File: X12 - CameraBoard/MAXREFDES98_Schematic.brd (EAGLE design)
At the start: 100 x 80 mm, 24 parts, among them U1 MB110S-TP, U2 MB110S-TP, U3 MAX5969AETB+, U4 MAX17503ATP+

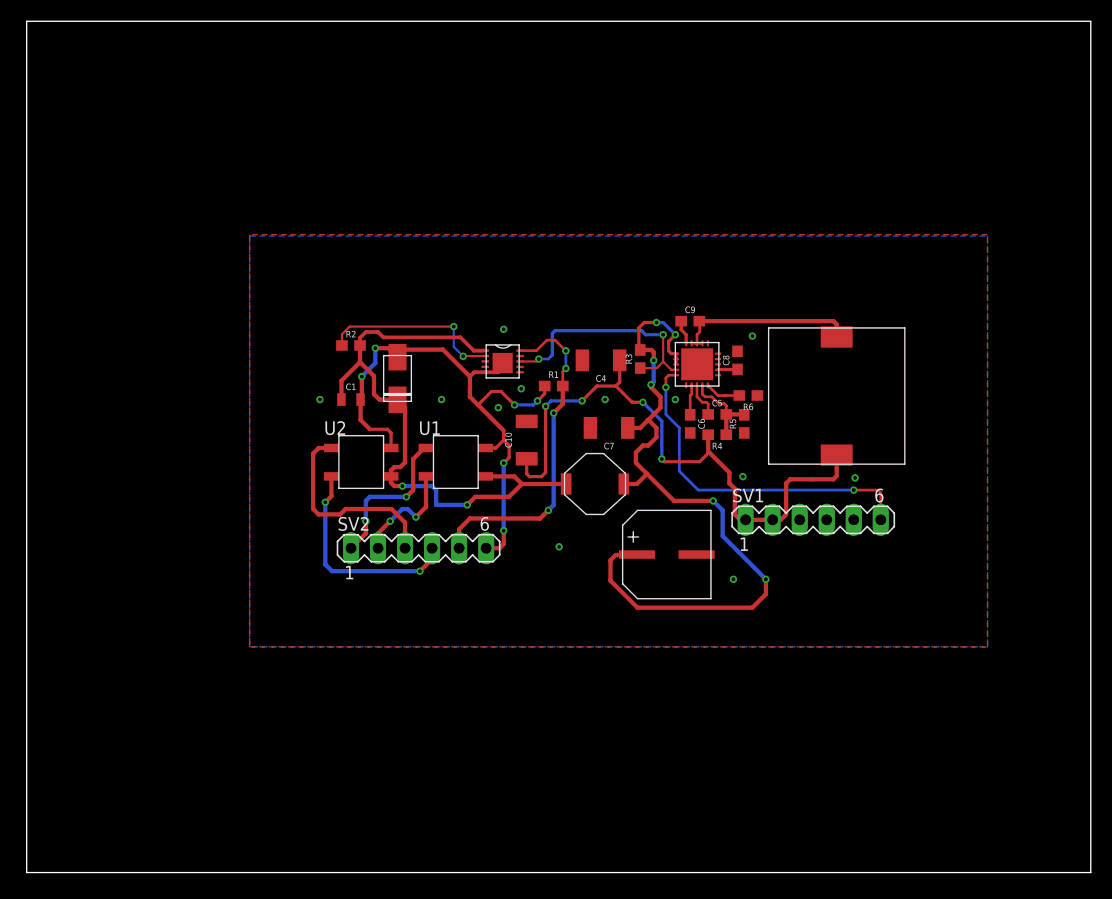
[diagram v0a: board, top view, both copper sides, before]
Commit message: Board Down-Scaling
Scaled board down to 500 mil in width and moved all large components to one side of the board.
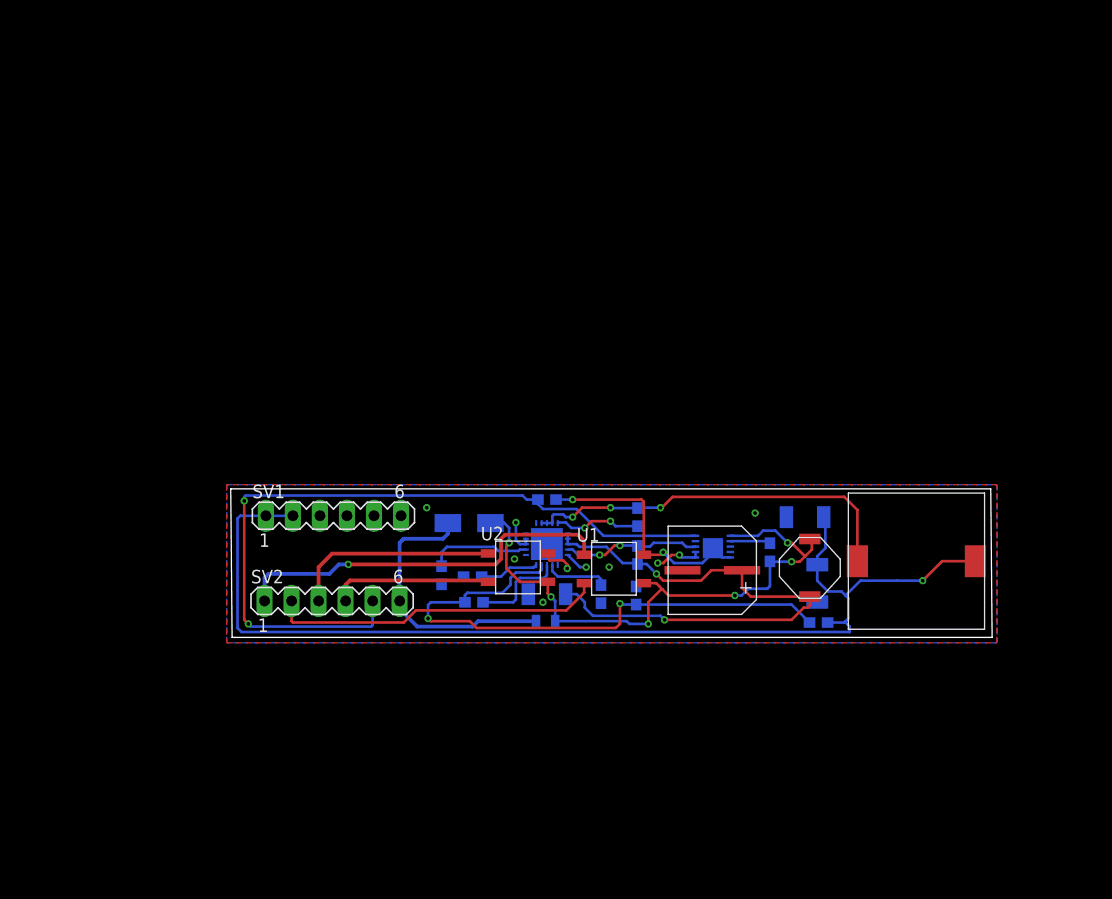
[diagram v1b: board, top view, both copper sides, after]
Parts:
- moved SV1 45.1 mm to (28.8, 33.5)
- moved R2 43.9 mm to (69.8, 30.1), flipped to the bottom, turned to 270 degrees
- moved C8 34.4 mm to (39.0, 27.9), flipped to the bottom, turned to 270 degrees
- moved R6 31.0 mm to (41.9, 27.8), flipped to the bottom
- moved C10 30.4 mm to (74.3, 27.2), flipped to the bottom, turned to 270 degrees
- moved L2 29.3 mm to (77.2, 22.9), turned to 0 degrees
- moved C5 28.9 mm to (42.0, 25.4), flipped to the bottom
- moved U3 28.7 mm to (66.0, 29.1), flipped to the bottom
- moved C1 27.7 mm to (48.8, 23.6), flipped to the bottom
- moved C4 24.2 mm to (73.2, 33.4), flipped to the bottom, turned to 0 degrees
- moved L1 20.3 mm to (70.7, 31.5), turned to 270 degrees
- moved R4 20.1 mm to (74.4, 23.5), flipped to the bottom
- moved U4 19.6 mm to (50.9, 28.8), flipped to the bottom
- moved C9 19.1 mm to (57.4, 33.4), flipped to the bottom, turned to 90 degrees
- moved R5 19.1 mm to (57.3, 26.0), flipped to the bottom, turned to 270 degrees
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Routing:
- net N$19: track 7.96 -> 53.6 mm, vias 0 -> 2
- net N$21: track 57.5 -> 101.9 mm, vias 4 -> 1
- net N$8: track 31.7 -> 70.7 mm, vias 4 -> 2
- net N$12: track 32.7 -> 2.20 mm
- net N$1: track 14.4 -> 36.5 mm, vias 2 -> 1
- net N$2: track 10.4 -> 31.5 mm, vias 2 -> 0
- net N$18: track 17.4 -> 36.8 mm, vias 0 -> 3
- net N$9: track 69.2 -> 53.2 mm, vias 6 -> 2
- net N$7: track 17.1 -> 3.80 mm, vias 2 -> 0
- net N$10: track 22.5 -> 12.9 mm
- net N$11: track 1.85 -> 9.66 mm
- net GND: track 0.00 -> 7.72 mm, vias 3 -> 7
- net N$17: track 2.28 -> 8.18 mm, vias 0 -> 2
- net N$14: track 3.40 -> 8.99 mm
- net N$4: track 20.3 -> 15.1 mm, vias 2 -> 0
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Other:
- board size 100 x 80 mm -> 71.6 x 14 mm

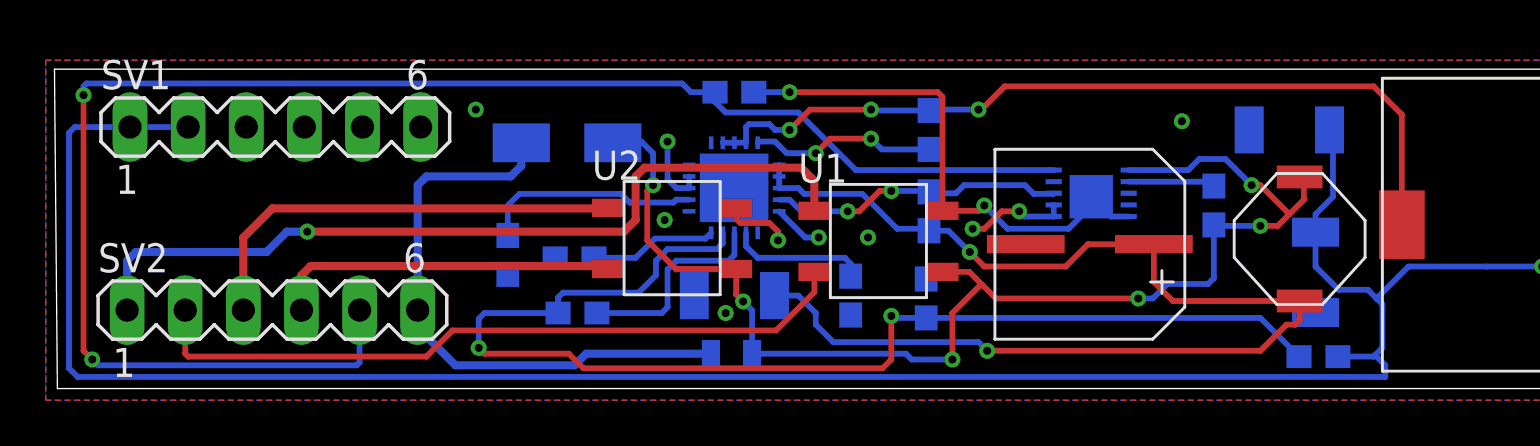
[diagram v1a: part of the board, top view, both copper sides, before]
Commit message: Update MAXREFDES98_Schematic.brd
Fixed Airwires and other misc. DRC errors.
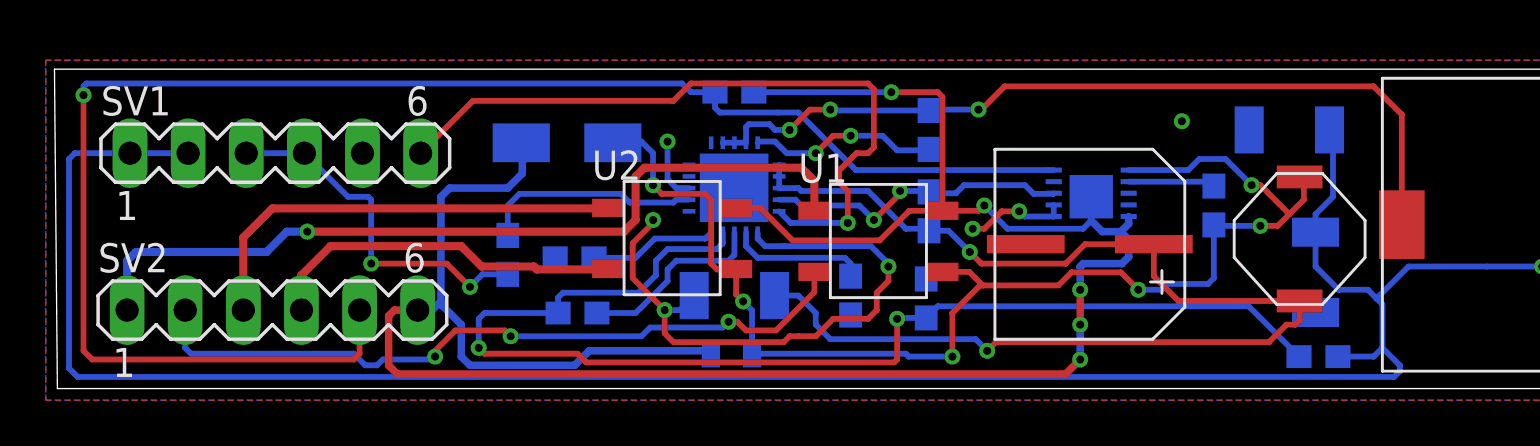
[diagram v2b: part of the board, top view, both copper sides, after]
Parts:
- moved SV1 1.14 mm to (28.8, 32.4)
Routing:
- net N$6: track 52.3 -> 101.0 mm, vias 3 -> 5
- net GND: track 7.72 -> 49.2 mm, vias 7 -> 9
- net N$12: track 2.20 -> 31.3 mm, vias 2 -> 1
- net N$2: track 31.5 -> 32.4 mm, vias 0 -> 3
- net N$4: track 15.1 -> 15.9 mm
- net N$14: track 8.99 -> 8.32 mm
- net N$8: track 70.7 -> 70.2 mm, vias 2 -> 1

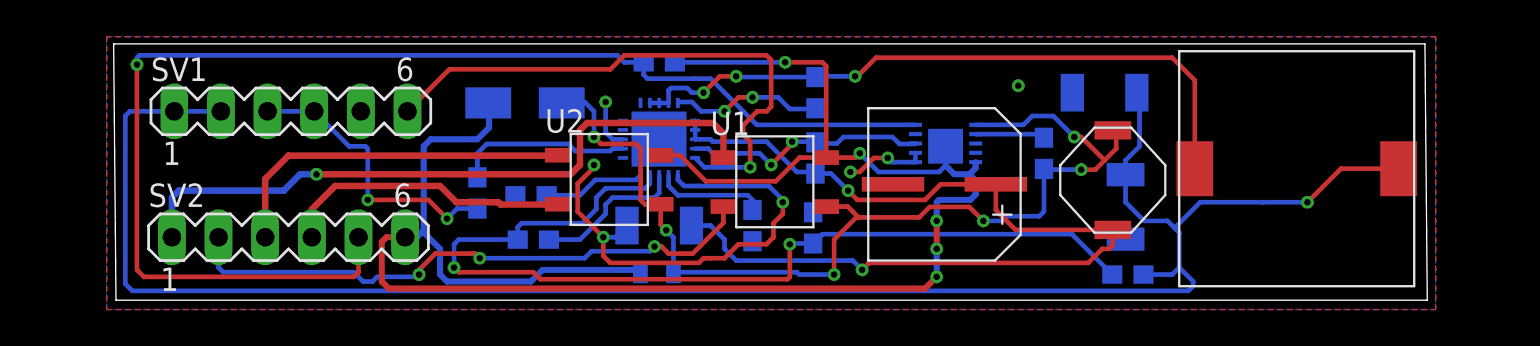
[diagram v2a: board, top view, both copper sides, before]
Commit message: Added Net Labels & Mounting Holes
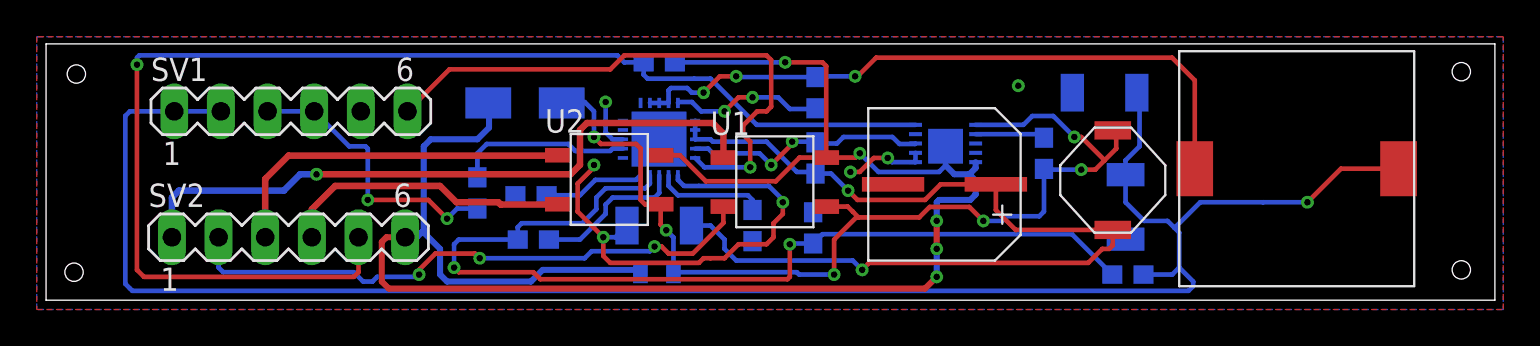
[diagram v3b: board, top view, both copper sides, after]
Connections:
- net N$1 renamed SV2_1
- net N$10 renamed PG_EN/UVLO
- net N$12 renamed RESET
- net N$13 renamed SS
- net N$14 renamed CF
- net N$16 renamed RT
- net N$17 renamed BST
- net N$18 renamed LX
- net N$19 renamed FB
- net N$2 renamed SV2_2
- net N$21 renamed SV1_1/2
- net N$25 renamed EPAD
- net N$3 renamed SV2_3
- net N$4 renamed SV2_4
- net N$5 renamed VDD
- net N$6 renamed VSS_EP
- net N$7 renamed DET
- net N$8 renamed CLS
- net N$9 renamed VIN
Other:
- board size 71.6 x 14 mm -> 78.9 x 14 mm

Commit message: rewiring
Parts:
- moved L1 30.1 mm to (44.2, 17.4)
- moved C8 27.3 mm to (22.0, 6.60)
- moved SV2 26.6 mm to (11.4, 5.33)
- moved C2 26.4 mm to (55.9, 1.14)
- moved C1 25.9 mm to (25.8, 11.7), turned to 90 degrees
- moved C5 25.8 mm to (25.9, 5.21)
- moved R6 25.5 mm to (26.0, 7.87)
- moved C7 25.4 mm to (32.9, 6.48)
- moved R4 23.5 mm to (52.6, 14.7)
- moved D1 23.2 mm to (29.1, 12.6)
- moved U1 23.2 mm to (35.9, 9.78)
- moved U2 23.2 mm to (26.9, 9.91)
- moved U4 23.2 mm to (35.2, 11.8)
- moved L2 21.7 mm to (61.6, 7.75)
- moved SV1 21.5 mm to (11.4, 19.7)
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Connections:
- net N$11 renamed VCC
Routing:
- net SV1_1/2: track 101.7 -> 0.00 mm, vias 1 -> 0
- net VSS_EP: track 101.0 -> 0.00 mm, vias 5 -> 0
- net VDD: track 55.6 -> 0.00 mm, vias 6 -> 0
- net FB: track 53.6 -> 0.00 mm, vias 2 -> 0
- net VIN: track 53.0 -> 0.00 mm, vias 2 -> 0
- net CLS: track 70.2 -> 18.3 mm, vias 1 -> 0
- net GND: track 49.2 -> 0.00 mm, vias 9 -> 0
- net LX: track 36.8 -> 0.00 mm, vias 3 -> 0
- net SV2_1: track 36.5 -> 0.00 mm, vias 1 -> 0
- net SV2_2: track 32.4 -> 0.00 mm, vias 3 -> 0
- net RESET: track 31.3 -> 0.00 mm, vias 1 -> 0
- net SV2_3: track 19.7 -> 0.00 mm
- net SV2_4: track 15.9 -> 0.00 mm
- net PG_EN/UVLO: track 13.3 -> 0.00 mm, vias 2 -> 0
- net VCC: track 9.66 -> 0.00 mm
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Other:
- board size 78.9 x 14 mm -> 78.9 x 25.4 mm

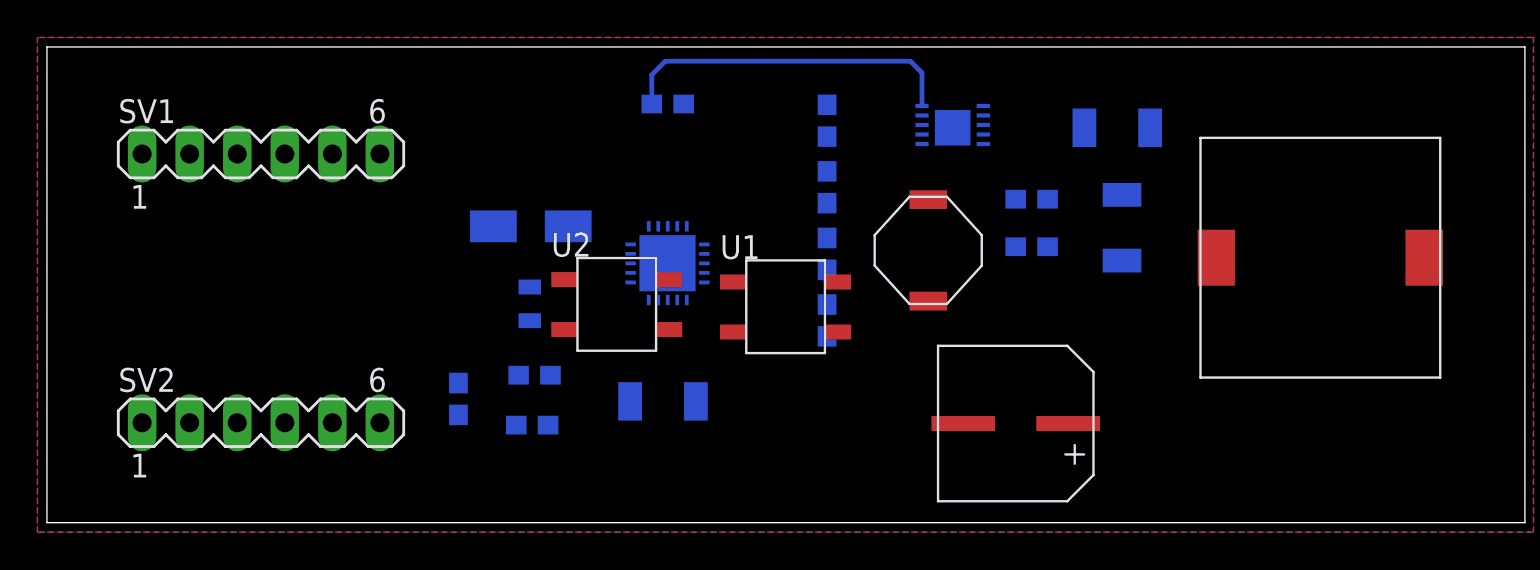
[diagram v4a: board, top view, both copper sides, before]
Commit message: Update MAXREFDES98_Schematic.brd
Changed mounting holes to be right size and place on board, according to NanoPi board.
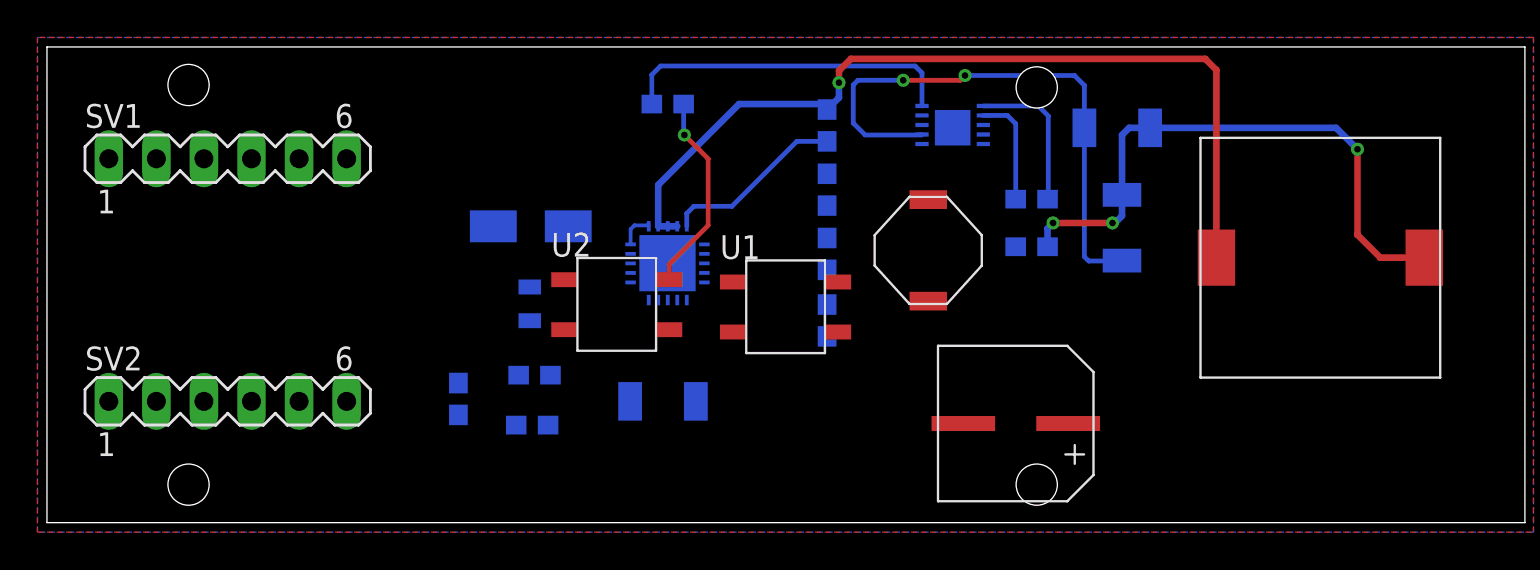
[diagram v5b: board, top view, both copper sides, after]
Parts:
- moved SV2 2.11 mm to (9.65, 6.48)
- moved SV1 1.80 mm to (9.65, 19.4)
- moved C9 0.25 mm to (41.7, 21.2)
- moved R3 0.13 mm to (41.7, 17.8)
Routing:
- net LX: track 0.00 -> 47.2 mm, vias 0 -> 1
- net GND: track 0.00 -> 31.9 mm, vias 0 -> 2
- net SV1_1/2: track 0.00 -> 31.4 mm, vias 0 -> 3
- net VSS_EP: track 0.00 -> 10.8 mm, vias 0 -> 1
- net BST: track 0.00 -> 9.77 mm
- net VDD: track 0.00 -> 8.15 mm
- net DET: track 0.00 -> 5.94 mm
